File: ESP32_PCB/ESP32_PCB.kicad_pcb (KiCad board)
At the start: 2 copper layers, 35 x 35 mm, 36 parts, among them J1 USB_C_Receptacle, J2 ESC1, J3 ESC2, J4 Conn_02x04_Counter_Clockwise, J5 LED, U2 H3LIS331DL, U3 AP2112K-3.3, U4 TPS54302, U5 ESP32-S3-MINI-1U

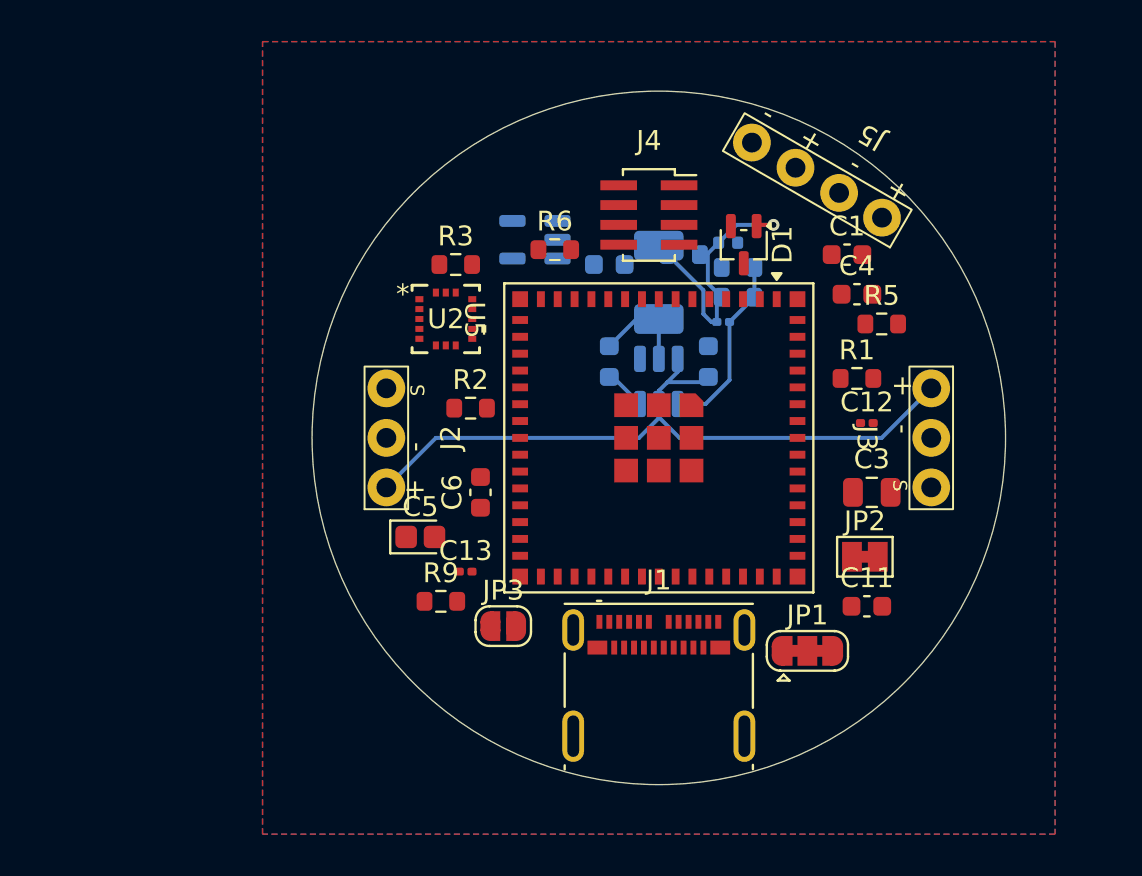
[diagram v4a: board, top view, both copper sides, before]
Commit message: Draw tracks for USB_D+ and  USB_D- nets
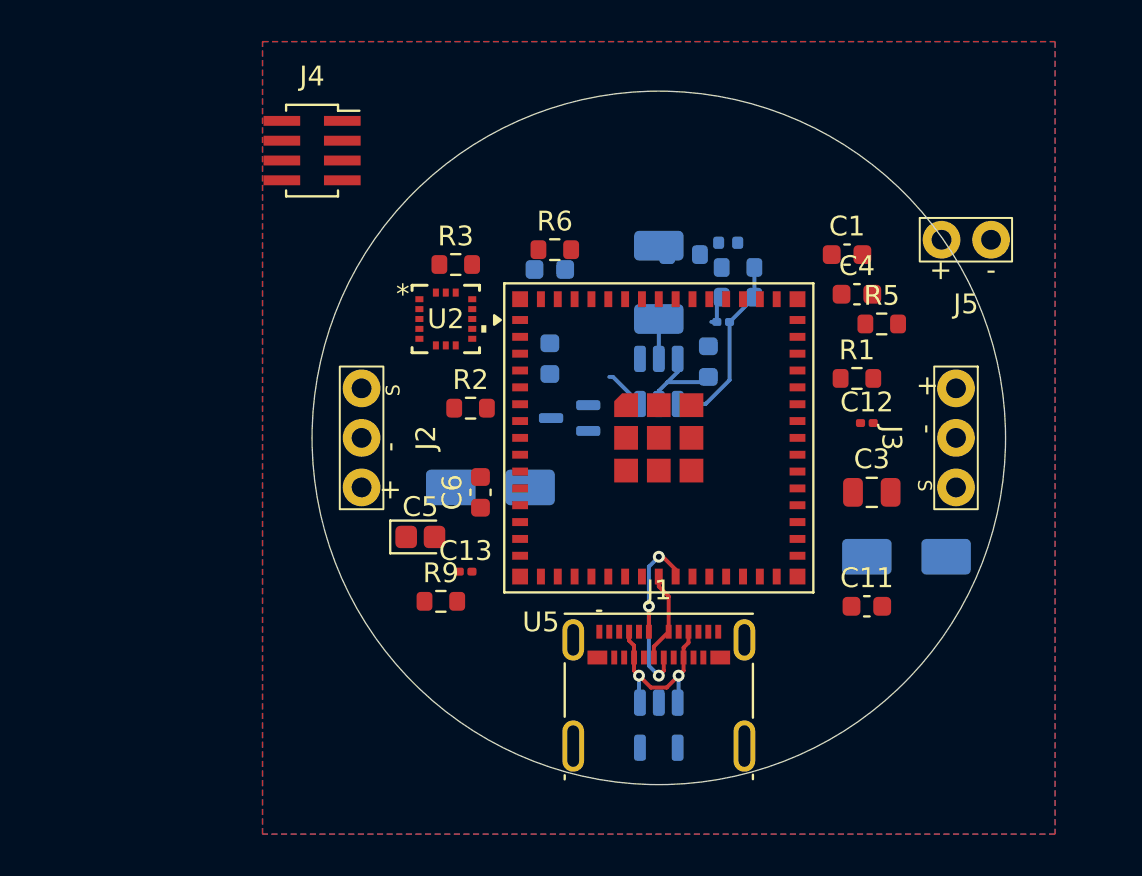
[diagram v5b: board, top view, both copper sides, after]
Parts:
- removed JP1: SolderJumper_3_Bridged123, Jumper:SolderJumper-3_P1.3mm_Bridged123_RoundedPad1.0x1.5mm
- removed JP2: SolderJumper_2_Bridged, Jumper:SolderJumper-2_P1.3mm_Bridged_Pad1.0x1.5mm
- removed JP3: SolderJumper_2_Open, Jumper:SolderJumper-2_P1.3mm_Open_RoundedPad1.0x1.5mm
- added D2: SMAJ36A, Diode_SMD:D_SMA, B.Cu at (141.5, 102.5)
- added D3: SMAJ36A, Diode_SMD:D_SMA, B.Cu at (162.5, 106.0)
- D1: moved to B.Cu
- J2: value ESC1 -> ESC 1
- J3: value ESC2 -> ESC 2
- J4: value Conn_02x04_Counter_Clockwise -> EN & Boot Switches
- J5: footprint ESC_Connectors:4_Pin -> ESC_Connectors:2_Pin
- moved U3 25.3 mm to (150.0, 114.5), turned to -90 degrees
- moved J4 17.3 mm to (132.5, 85.5)
- moved D1 12.4 mm to (145.5, 99.0), turned to 180 degrees
- moved J5 6.82 mm to (165.5, 90.0), turned to 0 degrees
- moved C2 3.01 mm to (144.5, 91.5)
- moved C8 3.00 mm to (144.5, 96.0)
- moved J2 1.25 mm to (135.0, 100.0)
- moved J3 1.25 mm to (165.0, 100.0)
- moved J1 0.50 mm to (150.0, 113.0)
- turned U5 to 0 degrees
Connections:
- net Net-(U5-USB_D+) renamed /USB_D+
- net Net-(U5-USB_D-) renamed /USB_D-
- J2 pad 1: VBATT -> Net-(D2-A2)
- J3 pad 1: VBATT -> Net-(D3-A2)
- R3 pad 1: Net-(JP1-B) -> +3V3
- R4 pad 1: Net-(JP1-A) -> +3V3
- R5 pad 2: /CS -> +3V3
- U2 pad 8: /CS -> +3V3
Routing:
- net VBATT: track 36.6 -> 4.84 mm
- net VIN: track 13.9 -> 1.63 mm, vias 1 -> 0
- net /USB_D+: track 0.00 -> 10.2 mm, vias 0 -> 3
- net Net-(U3-EN): track 0.00 -> 10.1 mm, vias 0 -> 2
- net /USB_D-: track 0.00 -> 4.60 mm
- net Net-(U4-SW): track 5.08 -> 3.14 mm

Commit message: Add tracks for buck converter and USB-C
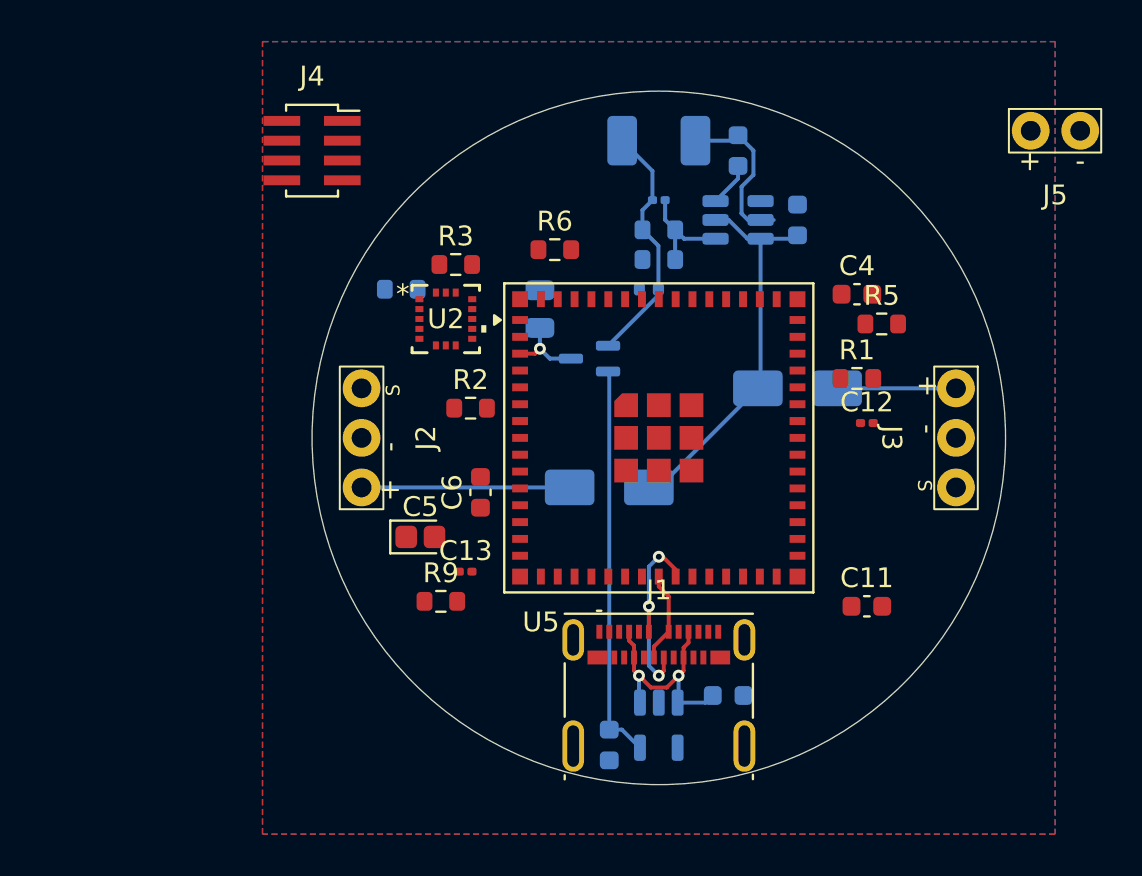
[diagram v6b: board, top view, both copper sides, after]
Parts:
- C1, C3: moved to B.Cu
- moved C1 27.5 mm to (147.5, 115.5), turned to 90 degrees
- moved C2 23.3 mm to (153.5, 113.0)
- moved C3 19.1 mm to (144.0, 93.5), turned to -90 degrees
- moved R4 14.4 mm to (137.0, 92.5)
- moved C8 14.2 mm to (154.0, 85.5)
- moved D3 10.1 mm to (157.0, 97.5), turned to 0 degrees
- moved U4 9.08 mm to (154.0, 89.0), turned to 180 degrees
- moved C7 8.45 mm to (157.0, 89.0)
- moved L1 7.15 mm to (150.0, 85.0), turned to 180 degrees
- moved J5 7.11 mm to (170.0, 84.5)
- moved C9 6.96 mm to (150.0, 88.0)
- moved D2 6.00 mm to (147.5, 102.5)
- moved R7 5.25 mm to (150.0, 89.5)
- moved C10 4.64 mm to (149.5, 92.5), turned to 0 degrees
- moved R8 4.02 mm to (150.0, 91.0)
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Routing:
- net /VUSB: track 0.00 -> 20.0 mm
- net VBATT: track 4.84 -> 19.8 mm
- net VIN: track 1.63 -> 12.6 mm
- net Net-(D2-A2): track 0.00 -> 10.5 mm
- net Net-(D3-A2): track 0.00 -> 6.00 mm
- net Net-(U4-SW): track 3.14 -> 8.54 mm
- net +3V3: track 0.00 -> 3.92 mm, vias 0 -> 1
- net Net-(U4-FB): track 9.32 -> 5.43 mm
- net Net-(U3-EN): track 10.1 -> 12.0 mm

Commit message: Finish EN & Boot header pins layout
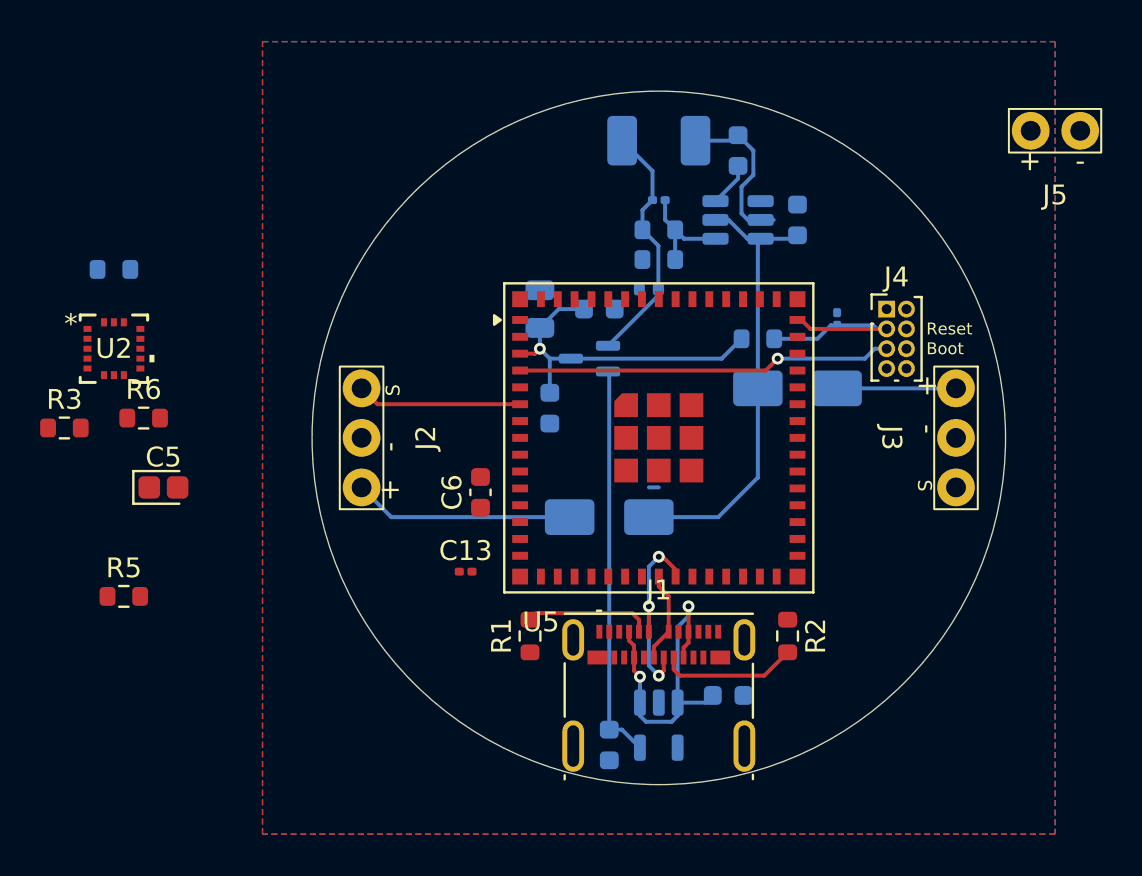
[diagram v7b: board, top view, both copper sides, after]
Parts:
- C11, C12, C4, R9: moved to B.Cu
- J4: value EN & Boot Switches -> EN & Boot; footprint Connector_PinSocket_1.00mm:PinSocket_2x04_P1.00mm_Vertical_SMD -> Connector_PinHeader_1.00mm:PinHeader_2x04_P1.00mm_Vertical
- moved R5 40.6 mm to (123.0, 108.0)
- moved J4 30.1 mm to (161.5, 93.5)
- moved R6 22.4 mm to (124.0, 99.0)
- moved R3 21.4 mm to (120.0, 99.5)
- moved R1 21.0 mm to (143.5, 110.0), turned to 90 degrees
- moved R9 20.8 mm to (155.0, 95.0), turned to 180 degrees
- moved C11 20.2 mm to (147.0, 93.5), turned to 180 degrees
- moved R2 19.7 mm to (156.5, 110.0), turned to -90 degrees
- moved U2 16.8 mm to (122.5, 95.5)
- moved C4 16.5 mm to (144.5, 98.5), turned to 90 degrees
- moved R4 14.5 mm to (122.5, 91.5)
- moved C5 13.2 mm to (125.0, 102.5)
- moved C12 5.46 mm to (159.0, 94.0), turned to -90 degrees
- moved D2 1.50 mm to (147.5, 104.0)
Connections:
- J4 pad 2: /EN -> GNDREF
- J4 pad 3: /BOOT -> /EN
- J4 pad 5: GNDREF -> /BOOT
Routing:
- net /BOOT: track 0.00 -> 19.0 mm, vias 0 -> 1
- net +3V3: track 3.92 -> 17.3 mm
- net /EN: track 0.00 -> 10.7 mm
- net /S1: track 0.00 -> 8.33 mm
- net Net-(J1-CC2): track 0.00 -> 6.97 mm
- net Net-(J1-CC1): track 0.00 -> 6.38 mm
- net Net-(U3-EN): track 12.0 -> 17.1 mm
- net VBATT: track 19.8 -> 23.5 mm
- net Net-(D2-A2): track 10.5 -> 11.1 mm
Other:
- board text added: "Boot"
- board text added: "Reset"

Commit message: Add tracks for S1, S2 and LED
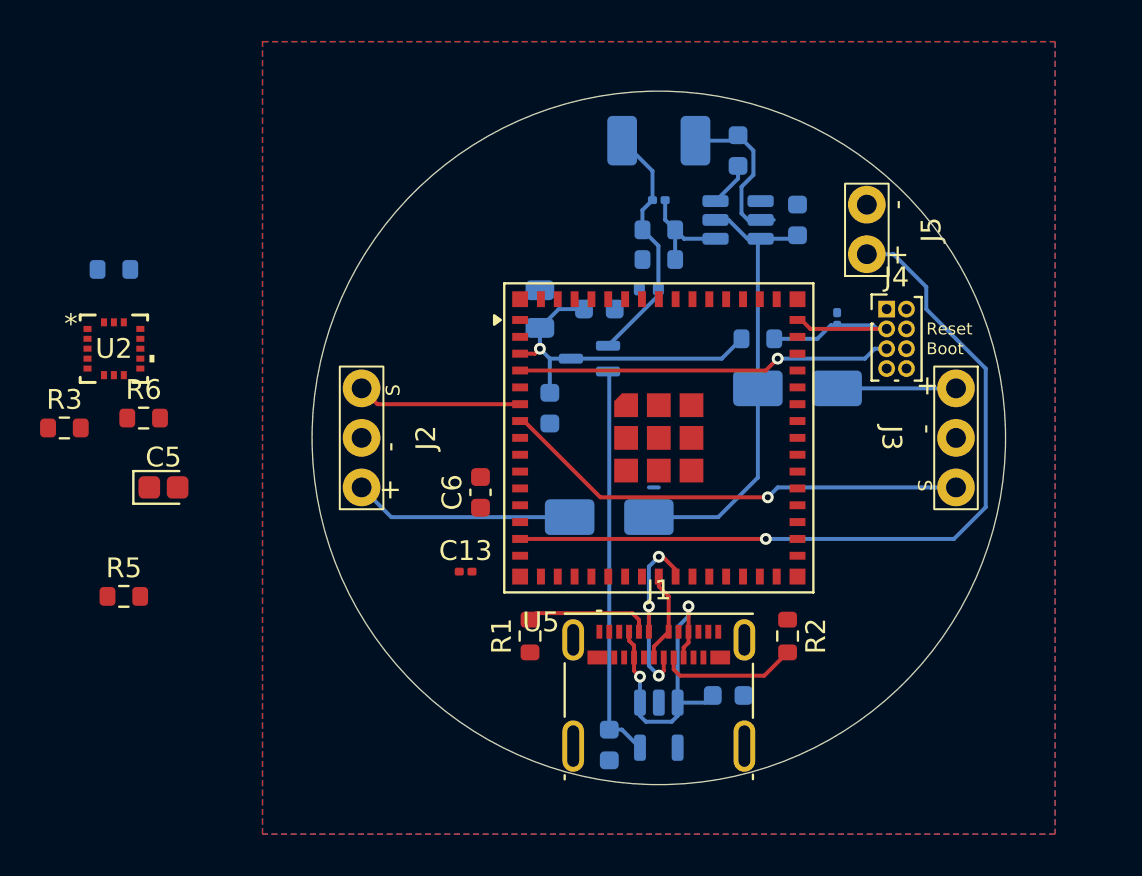
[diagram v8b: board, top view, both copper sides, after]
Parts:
- moved J5 10.7 mm to (160.5, 89.5), turned to 90 degrees
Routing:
- net /LED: track 0.00 -> 40.2 mm, vias 0 -> 1
- net /S2: track 0.00 -> 23.8 mm, vias 0 -> 1
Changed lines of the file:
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@@
 	(footprint "ESC_Connectors:2_Pin"
 		(layer "F.Cu")
-		(at 170 84.5)
+		(at 160.5 89.5 90)
 		(property "Reference" "J5"
-			(at 0 3.25 0)
+			(at 0 3.25 90)
 			(unlocked yes)
 			(layer "F.SilkS")
@@
 		)
 		(property "Value" "LED"
-			(at 0 -4.2 0)
+			(at 0 -4.2 90)
 			(unlocked yes)
 			(layer "F.Fab")
@@
 		)
 		(property "Datasheet" "~"
-			(at 0 0 0)
+			(at 0 0 90)
 			(unlocked yes)
 			(layer "F.Fab")
@@
 		)
 		(property "Description" "Generic connector, single row, 01x02, script generated (kicad-library-utils/schlib/autogen/connector/)"
-			(at 0 0 0)
+			(at 0 0 90)
 			(unlocked yes)
 			(layer "F.Fab")
@@
 		)
 		(fp_text user "+"
-			(at -1.27 1.524 0)
+			(at -1.27 1.524 90)
 			(unlocked yes)
 			(layer "F.SilkS")
@@
 		)
 		(fp_text user "-"
-			(at 1.27 1.524 0)
+			(at 1.27 1.524 90)
 			(unlocked yes)
 			(layer "F.SilkS")
@@
 		)
 		(fp_text user "2_Pin"
-			(at 0 -2.4 0)
+			(at 0 -2.4 90)
 			(unlocked yes)
 			(layer "F.Fab")
@@
 		)
 		(pad "1" thru_hole circle
-			(at -1.23 0)
+			(at -1.23 0 90)
 			(size 1.905 1.905)
 			(drill 1)
@@
 		)
 		(pad "2" thru_hole circle
-			(at 1.27 0)
+			(at 1.27 0 90)
 			(size 1.905 1.905)
 			(drill 1)
@@
 			(polygon
 				(pts
-					(xy 167.77 83.5) (xy 172.23 83.5) (xy 172.23 85.5) (xy 167.77 85.5)
+					(xy 159.5 91.73) (xy 159.5 87.27) (xy 161.5 87.27) (xy 161.5 91.73)
 				)
 			)
@@
 	)
 	(segment
+		(start 143 99.15)
+		(end 143.2 99.15)
+		(width 0.2)
+		(layer "F.Cu")
+		(net 27)
+	)
+	(segment
+		(start 147.05 103)
+		(end 155.5 103)
+		(width 0.2)
+		(layer "F.Cu")
+		(net 27)
+	)
+	(segment
+		(start 143.2 99.15)
+		(end 147.05 103)
+		(width 0.2)
+		(layer "F.Cu")
+		(net 27)
+	)
+	(via
+		(at 155.5 103)
+		(size 0.6)
+		(drill 0.3)
+		(layers "F.Cu" "B.Cu")
+		(net 27)
+	)
+	(segment
+		(start 155.5 103)
+		(end 156 102.5)
+		(width 0.2)
+		(layer "B.Cu")
+		(net 27)
+	)
+	(segment
+		(start 156 102.5)
+		(end 165 102.5)
+		(width 0.2)
+		(layer "B.Cu")
+		(net 27)
+	)
+	(segment
 		(start 136.5 104)
 		(end 135 102.5)
@@
 	)
 	(segment
+		(start 143 105.1)
+		(end 155.4 105.1)
+		(width 0.2)
+		(layer "F.Cu")
+		(net 67)
+	)
+	(via
+		(at 155.4 105.1)
+		(size 0.6)
+		(drill 0.3)
+		(layers "F.Cu" "B.Cu")
+		(net 67)
+	)
+	(segment
+		(start 166.5 103.5)
+		(end 164.9 105.1)
+		(width 0.2)
+		(layer "B.Cu")
+		(net 67)
+	)
+	(segment
+		(start 163.5 92.382962)
+		(end 163.5 93.5)
+		(width 0.2)
+		(layer "B.Cu")
+		(net 67)
+	)
+	(segment
+		(start 161.847038 90.73)
+		(end 163.5 92.382962)
+		(width 0.2)
+		(layer "B.Cu")
+		(net 67)
+	)
+	(segment
+		(start 163.5 93.5)
+		(end 166.5 96.5)
+		(width 0.2)
+		(layer "B.Cu")
+		(net 67)
+	)
+	(segment
+		(start 166.5 96.5)
+		(end 166.5 103.5)
+		(width 0.2)
+		(layer "B.Cu")
+		(net 67)
+	)
+	(segment
+		(start 160.5 90.73)
+		(end 161.847038 90.73)
+		(width 0.2)
+		(layer "B.Cu")
+		(net 67)
+	)
+	(segment
+		(start 164.9 105.1)
+		(end 155.4 105.1)
+		(width 0.2)
+		(layer "B.Cu")
+		(net 67)
+	)
+	(segment
